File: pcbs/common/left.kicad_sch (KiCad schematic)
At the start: 89 parts, among them J2 TRS

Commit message: first pass at the gecko
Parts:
- removed EXLED? (x2): YS-SK6812MINI-E, kbd_local:YS-SK6812MINI-E, symbol kbd_local:YS-SK6812MINI-E
- removed EXSW? (x2): RotaryEncoder_Switch, kbd_local:keyswitch_cherrymx_hotswap_1u_rotary_encoder_ec12, symbol Device:RotaryEncoder_Switch
- added EXLED1, EXLED2: YS-SK6812MINI-E, kbd_local:YS-SK6812MINI-E, symbol kbd_local:YS-SK6812MINI-E
- added RE1, RE2: RotaryEncoder, kbd:rotary_encoder_EC05E_Vert, symbol Device:RotaryEncoder
- added RE1-2, RE1-3, RE2-2, RE2-3: RotaryEncoder, kbd:rotary_encoder_EC05E, symbol Device:RotaryEncoder
- added SW22, SW23: SW_Push, kbd:keyswitch_cherrymx_hotswap_1u, symbol Switch:SW_Push
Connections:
- net GND: now also EXLED1.3 (VSS), EXLED2.3 (VSS), RE1-2.C, RE1-3.C, RE1.C, RE2-2.C, RE2-3.C, RE2.C, SW22.2, SW23.2
- net RE0A: now also RE1-2.A, RE1-3.A, RE1.A
- net RE1A: now also RE2-2.A, RE2-3.A, RE2.A
- net REB: now also RE1-2.B, RE1-3.B, RE1.B, RE2-2.B, RE2-3.B, RE2.B
- net at D?.1 (K), LED?.1 (VDD), LED?.1 (VDD)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: now also EXLED1.1 (VDD), EXLED2.1 (VDD)
- net at LED?.4 (DIN): now also EXLED1.2 (DOUT); no longer LED?.2 (DOUT)
- net KEYEX1 renamed KEY22
- net KEY22: now also SW22.1
- net KEYEX2 renamed KEY23
- net KEY23: now also SW23.1
- new net: EXLED1.4 (DIN), EXLED2.2 (DOUT)
- new net: EXLED2.4 (DIN), LED?.2 (DOUT)

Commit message: moved subsheets across
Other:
- company: foostan -> Dane Evans
- title: Corne Left -> Gecko Left
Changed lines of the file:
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@@
 	(paper "A3")
 	(title_block
-		(title "Corne Left")
+		(title "Gecko Left")
 		(date "2023-10-07")
-		(rev "4.0.0")
-		(company "foostan")
+		(rev "1.0.0")
+		(company "Dane Evans")
+		(comment 1 "original: foostan's crkbd 4.1")
 	)
 	(junction
@@
 		)
 		(instances
-			(project "corne-chocolate"
+			(project "Gecko_choc"
 				(path "/4cc5d416-57f5-4147-8183-e03ae6b1198a/089db7cd-2934-428b-a62a-55e0735649ba"
 					(reference "SW22")
@@
 		)
 		(instances
-			(project "corne-chocolate"
+			(project "Gecko_choc"
 				(path "/4cc5d416-57f5-4147-8183-e03ae6b1198a/089db7cd-2934-428b-a62a-55e0735649ba"
 					(reference "SW23")
@@
 		)
 		(instances
-			(project "corne-chocolate"
+			(project "Gecko_choc"
 				(path "/4cc5d416-57f5-4147-8183-e03ae6b1198a/089db7cd-2934-428b-a62a-55e0735649ba"
 					(reference "#PWR057")
@@
 		)
 		(instances
-			(project "corne-cherry"
+			(project "Gecko_choc"
 				(path "/4cc5d416-57f5-4147-8183-e03ae6b1198a/089db7cd-2934-428b-a62a-55e0735649ba"
 					(reference "BT2")
@@
 		)
 		(instances
-			(project "corne-chocolate"
+			(project "Gecko_choc"
 				(path "/4cc5d416-57f5-4147-8183-e03ae6b1198a/089db7cd-2934-428b-a62a-55e0735649ba"
 					(reference "#PWR056")
@@
 		)
 		(instances
-			(project "corne-chocolate"
+			(project "Gecko_choc"
 				(path "/4cc5d416-57f5-4147-8183-e03ae6b1198a/089db7cd-2934-428b-a62a-55e0735649ba"
 					(reference "#PWR081")
@@
 		)
 		(instances
-			(project "corne-chocolate"
+			(project "Gecko_choc"
 				(path "/4cc5d416-57f5-4147-8183-e03ae6b1198a/089db7cd-2934-428b-a62a-55e0735649ba"
 					(reference "RE2-3")
@@
 		)
 		(instances
-			(project "corne-cherry"
+			(project "Gecko_choc"
 				(path "/4cc5d416-57f5-4147-8183-e03ae6b1198a/089db7cd-2934-428b-a62a-55e0735649ba"
 					(reference "JP1")
@@
 		)
 		(instances
-			(project "corne-chocolate"
+			(project "Gecko_choc"
 				(path "/4cc5d416-57f5-4147-8183-e03ae6b1198a/089db7cd-2934-428b-a62a-55e0735649ba"
 					(reference "EXLED1")
@@
 		)
 		(instances
-			(project "corne-chocolate"
+			(project "Gecko_choc"
 				(path "/4cc5d416-57f5-4147-8183-e03ae6b1198a/089db7cd-2934-428b-a62a-55e0735649ba"
 					(reference "EXLED2")
@@
 		)
 		(instances
-			(project "corne-cherry"
+			(project "Gecko_choc"
 				(path "/4cc5d416-57f5-4147-8183-e03ae6b1198a/089db7cd-2934-428b-a62a-55e0735649ba"
 					(reference "BT3")
@@
 		)
 		(instances
-			(project "corne-chocolate"
+			(project "Gecko_choc"
 				(path "/4cc5d416-57f5-4147-8183-e03ae6b1198a/089db7cd-2934-428b-a62a-55e0735649ba"
 					(reference "#PWR055")
@@
 		)
 		(instances
-			(project "corne-cherry"
+			(project "Gecko_choc"
 				(path "/4cc5d416-57f5-4147-8183-e03ae6b1198a/089db7cd-2934-428b-a62a-55e0735649ba"
 					(reference "BT4")
@@
 		)
 		(instances
-			(project ""
+			(project "Gecko_choc"
 				(path "/4cc5d416-57f5-4147-8183-e03ae6b1198a/089db7cd-2934-428b-a62a-55e0735649ba"
 					(reference "RE1")
@@
 		)
 		(instances
-			(project "corne-chocolate"
+			(project "Gecko_choc"
 				(path "/4cc5d416-57f5-4147-8183-e03ae6b1198a/089db7cd-2934-428b-a62a-55e0735649ba"
 					(reference "#PWR064")
@@
 		)
 		(instances
-			(project "corne-chocolate"
+			(project "Gecko_choc"
 				(path "/4cc5d416-57f5-4147-8183-e03ae6b1198a/089db7cd-2934-428b-a62a-55e0735649ba"
 					(reference "RE2-2")
@@
 		)
 		(instances
-			(project "corne-chocolate"
+			(project "Gecko_choc"
 				(path "/4cc5d416-57f5-4147-8183-e03ae6b1198a/089db7cd-2934-428b-a62a-55e0735649ba"
 					(reference "#PWR080")
@@
 		)
 		(instances
-			(project "corne-chocolate"
+			(project "Gecko_choc"
 				(path "/4cc5d416-57f5-4147-8183-e03ae6b1198a/089db7cd-2934-428b-a62a-55e0735649ba"
 					(reference "RE1-2")
@@
 		)
 		(instances
-			(project "corne-chocolate"
+			(project "Gecko_choc"
 				(path "/4cc5d416-57f5-4147-8183-e03ae6b1198a/089db7cd-2934-428b-a62a-55e0735649ba"
 					(reference "#PWR063")
@@
 		)
 		(instances
-			(project "corne-chocolate"
+			(project "Gecko_choc"
 				(path "/4cc5d416-57f5-4147-8183-e03ae6b1198a/089db7cd-2934-428b-a62a-55e0735649ba"
 					(reference "RE1-3")
@@
 		)
 		(instances
-			(project "corne-cherry"
+			(project "Gecko_choc"
 				(path "/4cc5d416-57f5-4147-8183-e03ae6b1198a/089db7cd-2934-428b-a62a-55e0735649ba"
 					(reference "J2")
@@
 		)
 		(instances
-			(project "corne-chocolate"
+			(project "Gecko_choc"
 				(path "/4cc5d416-57f5-4147-8183-e03ae6b1198a/089db7cd-2934-428b-a62a-55e0735649ba"
 					(reference "RE2")
@@
 		)
 		(instances
-			(project "corne-cherry"
+			(project "Gecko_choc"
 				(path "/4cc5d416-57f5-4147-8183-e03ae6b1198a/089db7cd-2934-428b-a62a-55e0735649ba"
 					(reference "BT1")

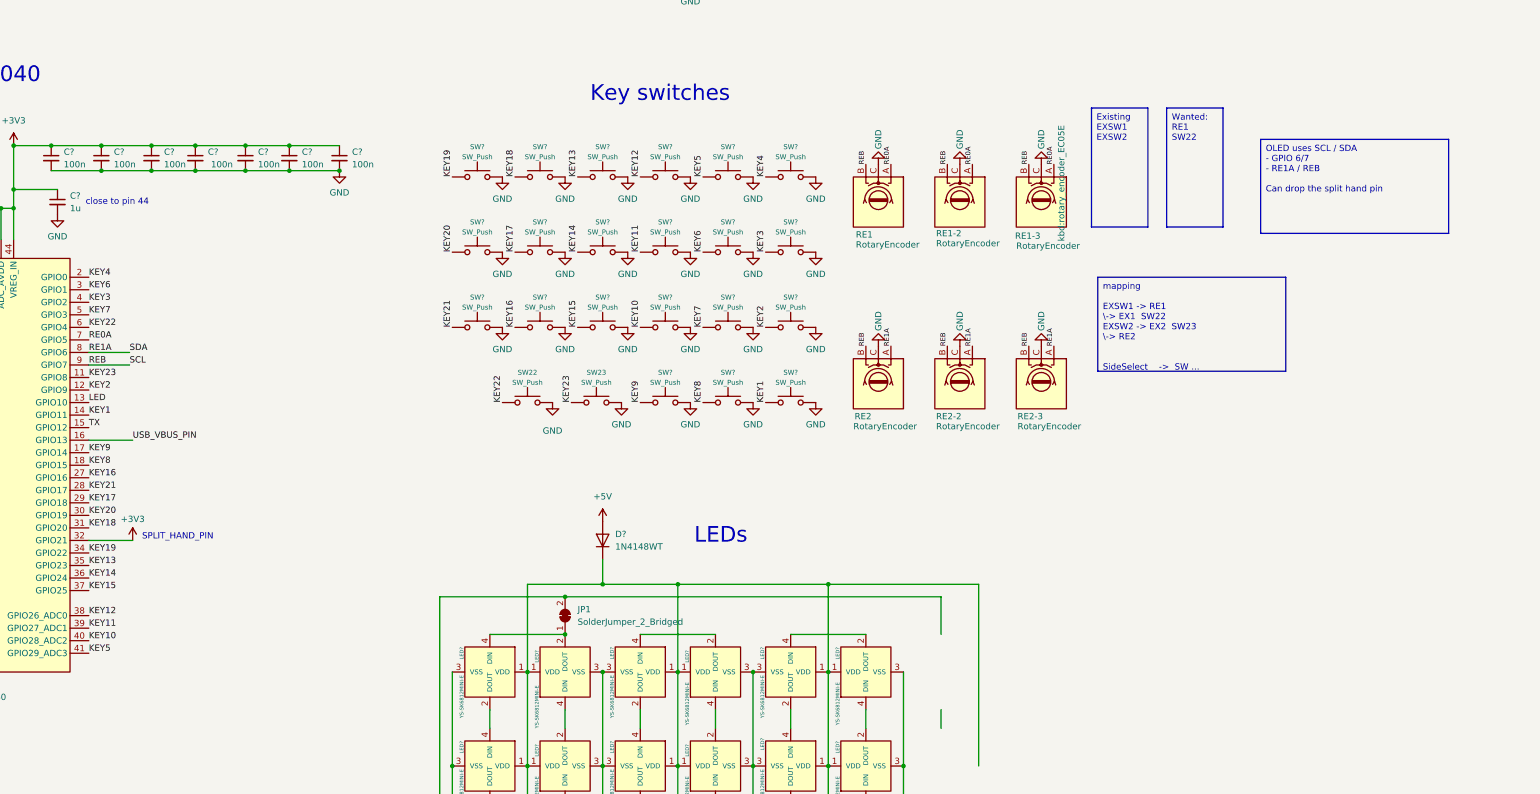
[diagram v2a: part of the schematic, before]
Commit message: add jumpers to the split pin
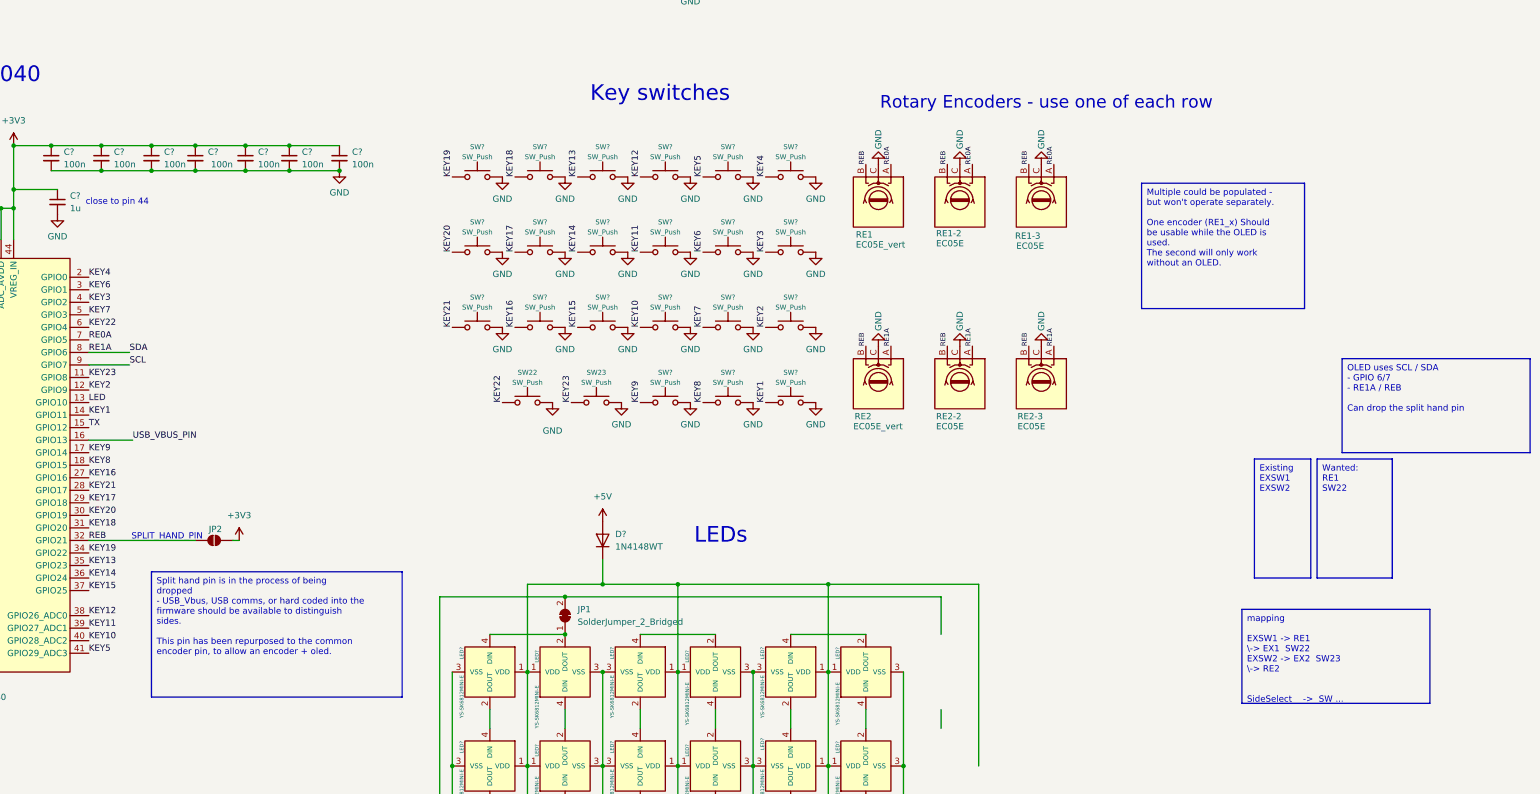
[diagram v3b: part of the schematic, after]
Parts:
- added JP2: SolderJumper_2_Open, Jumper:SolderJumper-2_P1.3mm_Open_RoundedPad1.0x1.5mm, symbol Jumper:SolderJumper_2_Open
- EXLED1, EXLED2, LED? (x21): footprint kbd_local:YS-SK6812MINI-E -> kbd:YS-SK6812MINI-E
- RE1, RE2: value RotaryEncoder -> EC05E_vert
- RE1-2, RE1-3, RE2-2, RE2-3: value RotaryEncoder -> EC05E
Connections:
- net +3V3: now also JP2.2 (B); no longer U?.32 (GPIO21)
- net REB: now also U?.32 (GPIO21), JP2.1 (A); no longer J?.2 (Pin_2), U?.9 (GPIO7)
- new net SCL: J?.2 (Pin_2), U?.9 (GPIO7)
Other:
- note added: "Rotary Encoders - use one of each row"

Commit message: allDRC
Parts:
- BT1, BT2, BT3, BT4: footprint kbd_local:Breakaway_Tabs -> kbd:Breakaway_Tabs
- J2: footprint kbd_local:PJ-398A-5A_PJ-399B-6A -> kbd:PJ-398A-5A_PJ-399B-6A
- J?: footprint kbd_local:OLED -> kbd:OLED
- J?: footprint kbd_local:TYPE-C-31-M-13C -> kbd:TYPE-C-31-M-13C
- SMDSW? (x2): footprint kbd_local:TS-1088R-02026 -> kbd:TS-1088R-02026
- SW22, SW23, SW? (x20): footprint kbd:keyswitch_cherrymx_hotswap_1u -> kbd:keyswitch_choc12_hotswap_1u
- SW?: footprint kbd:keyswitch_cherrymx_hotswap_1.5u -> kbd:keyswitch_choc12_hotswap_1.5u
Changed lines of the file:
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@@
 			)
 		)
-		(property "Footprint" "kbd:keyswitch_cherrymx_hotswap_1u"
+		(property "Footprint" "kbd:keyswitch_choc12_hotswap_1u"
 			(at 241.3 102.87 0)
 			(effects
@@
 			)
 		)
-		(property "Footprint" "kbd:keyswitch_cherrymx_hotswap_1u"
+		(property "Footprint" "kbd:keyswitch_choc12_hotswap_1u"
 			(at 254 102.87 0)
 			(effects
@@
 			)
 		)
-		(property "Footprint" "kbd:keyswitch_cherrymx_hotswap_1u"
+		(property "Footprint" "kbd:keyswitch_choc12_hotswap_1u"
 			(at 228.6 102.87 0)
 			(effects
@@
 			)
 		)
-		(property "Footprint" "kbd:keyswitch_cherrymx_hotswap_1u"
+		(property "Footprint" "kbd:keyswitch_choc12_hotswap_1u"
 			(at 241.3 133.35 0)
 			(effects
@@
 			)
 		)
-		(property "Footprint" "kbd:keyswitch_cherrymx_hotswap_1u"
+		(property "Footprint" "kbd:keyswitch_choc12_hotswap_1u"
 			(at 190.5 133.35 0)
 			(effects
@@
 			)
 		)
-		(property "Footprint" "kbd:keyswitch_cherrymx_hotswap_1u"
+		(property "Footprint" "kbd:keyswitch_choc12_hotswap_1u"
 			(at 200.66 148.59 0)
 			(effects
@@
 			)
 		)
-		(property "Footprint" "kbd:keyswitch_cherrymx_hotswap_1u"
+		(property "Footprint" "kbd:keyswitch_choc12_hotswap_1u"
 			(at 190.5 102.87 0)
 			(effects
@@
 			)
 		)
-		(property "Footprint" "kbd:keyswitch_cherrymx_hotswap_1u"
+		(property "Footprint" "kbd:keyswitch_choc12_hotswap_1u"
 			(at 241.3 118.11 0)
 			(effects
@@
 			)
 		)
-		(property "Footprint" "kbd:keyswitch_cherrymx_hotswap_1u"
+		(property "Footprint" "kbd:keyswitch_choc12_hotswap_1u"
 			(at 214.63 148.59 0)
 			(effects
@@
 			)
 		)
-		(property "Footprint" "kbd:keyswitch_cherrymx_hotswap_1.5u"
+		(property "Footprint" "kbd:keyswitch_choc12_hotswap_1.5u"
 			(at 254 148.59 0)
 			(effects
@@
 			)
 		)
-		(property "Footprint" "kbd:keyswitch_cherrymx_hotswap_1u"
+		(property "Footprint" "kbd:keyswitch_choc12_hotswap_1u"
 			(at 215.9 118.11 0)
 			(effects
@@
 			)
 		)
-		(property "Footprint" "kbd_local:Breakaway_Tabs"
+		(property "Footprint" "kbd:Breakaway_Tabs"
 			(at 17.78 264.16 0)
 			(effects
@@
 			)
 		)
-		(property "Footprint" "kbd:keyswitch_cherrymx_hotswap_1u"
+		(property "Footprint" "kbd:keyswitch_choc12_hotswap_1u"
 			(at 203.2 118.11 0)
 			(effects
@@
 			)
 		)
-		(property "Footprint" "kbd:keyswitch_cherrymx_hotswap_1u"
+		(property "Footprint" "kbd:keyswitch_choc12_hotswap_1u"
 			(at 203.2 133.35 0)
 			(effects
@@
 			)
 		)
-		(property "Footprint" "kbd:keyswitch_cherrymx_hotswap_1u"
+		(property "Footprint" "kbd:keyswitch_choc12_hotswap_1u"
 			(at 215.9 133.35 0)
 			(effects
@@
 			)
 		)
-		(property "Footprint" "kbd:keyswitch_cherrymx_hotswap_1u"
+		(property "Footprint" "kbd:keyswitch_choc12_hotswap_1u"
 			(at 203.2 102.87 0)
 			(effects
@@
 			)
 		)
-		(property "Footprint" "kbd:keyswitch_cherrymx_hotswap_1u"
+		(property "Footprint" "kbd:keyswitch_choc12_hotswap_1u"
 			(at 254 133.35 0)
 			(effects
@@
 			)
 		)
-		(property "Footprint" "kbd_local:Breakaway_Tabs"
+		(property "Footprint" "kbd:Breakaway_Tabs"
 			(at 17.78 270.51 0)
 			(effects
@@
 			)
 		)
-		(property "Footprint" "kbd_local:OLED"
+		(property "Footprint" "kbd:OLED"
 			(at 308.61 44.45 0)
 			(effects
@@
 			)
 		)
-		(property "Footprint" "kbd_local:Breakaway_Tabs"
+		(property "Footprint" "kbd:Breakaway_Tabs"
 			(at 17.78 276.86 0)
 			(effects
@@
 			)
 		)
-		(property "Footprint" "kbd_local:TYPE-C-31-M-13C"
+		(property "Footprint" "kbd:TYPE-C-31-M-13C"
 			(at 39.37 48.26 0)
 			(effects
@@
 			)
 		)
-		(property "Footprint" "kbd:keyswitch_cherrymx_hotswap_1u"
+		(property "Footprint" "kbd:keyswitch_choc12_hotswap_1u"
 			(at 228.6 118.11 0)
 			(effects
@@
 			)
 		)
-		(property "Footprint" "kbd:keyswitch_cherrymx_hotswap_1u"
+		(property "Footprint" "kbd:keyswitch_choc12_hotswap_1u"
 			(at 190.5 118.11 0)
 			(effects
@@
 			)
 		)
-		(property "Footprint" "kbd:keyswitch_cherrymx_hotswap_1u"
+		(property "Footprint" "kbd:keyswitch_choc12_hotswap_1u"
 			(at 215.9 102.87 0)
 			(effects
@@
 			)
 		)
-		(property "Footprint" "kbd_local:TS-1088R-02026"
+		(property "Footprint" "kbd:TS-1088R-02026"
 			(at 195.58 43.18 0)
 			(effects
@@
 			)
 		)
-		(property "Footprint" "kbd:keyswitch_cherrymx_hotswap_1u"
+		(property "Footprint" "kbd:keyswitch_choc12_hotswap_1u"
 			(at 241.3 148.59 0)
 			(effects
@@
 			)
 		)
-		(property "Footprint" "kbd_local:TS-1088R-02026"
+		(property "Footprint" "kbd:TS-1088R-02026"
 			(at 55.88 123.19 0)
 			(effects
@@
 			)
 		)
-		(property "Footprint" "kbd:keyswitch_cherrymx_hotswap_1u"
+		(property "Footprint" "kbd:keyswitch_choc12_hotswap_1u"
 			(at 228.6 148.59 0)
 			(effects
@@
 			)
 		)
-		(property "Footprint" "kbd:keyswitch_cherrymx_hotswap_1u"
+		(property "Footprint" "kbd:keyswitch_choc12_hotswap_1u"
 			(at 254 118.11 0)
 			(effects
@@
 			)
 		)
-		(property "Footprint" "kbd_local:PJ-398A-5A_PJ-399B-6A"
+		(property "Footprint" "kbd:PJ-398A-5A_PJ-399B-6A"
 			(at 272.415 36.83 0)
 			(effects
@@
 			)
 		)
-		(property "Footprint" "kbd:keyswitch_cherrymx_hotswap_1u"
+		(property "Footprint" "kbd:keyswitch_choc12_hotswap_1u"
 			(at 228.6 133.35 0)
 			(effects
@@
 			)
 		)
-		(property "Footprint" "kbd_local:Breakaway_Tabs"
+		(property "Footprint" "kbd:Breakaway_Tabs"
 			(at 17.78 257.81 0)
 			(effects
